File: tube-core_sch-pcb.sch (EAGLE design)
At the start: 14 parts

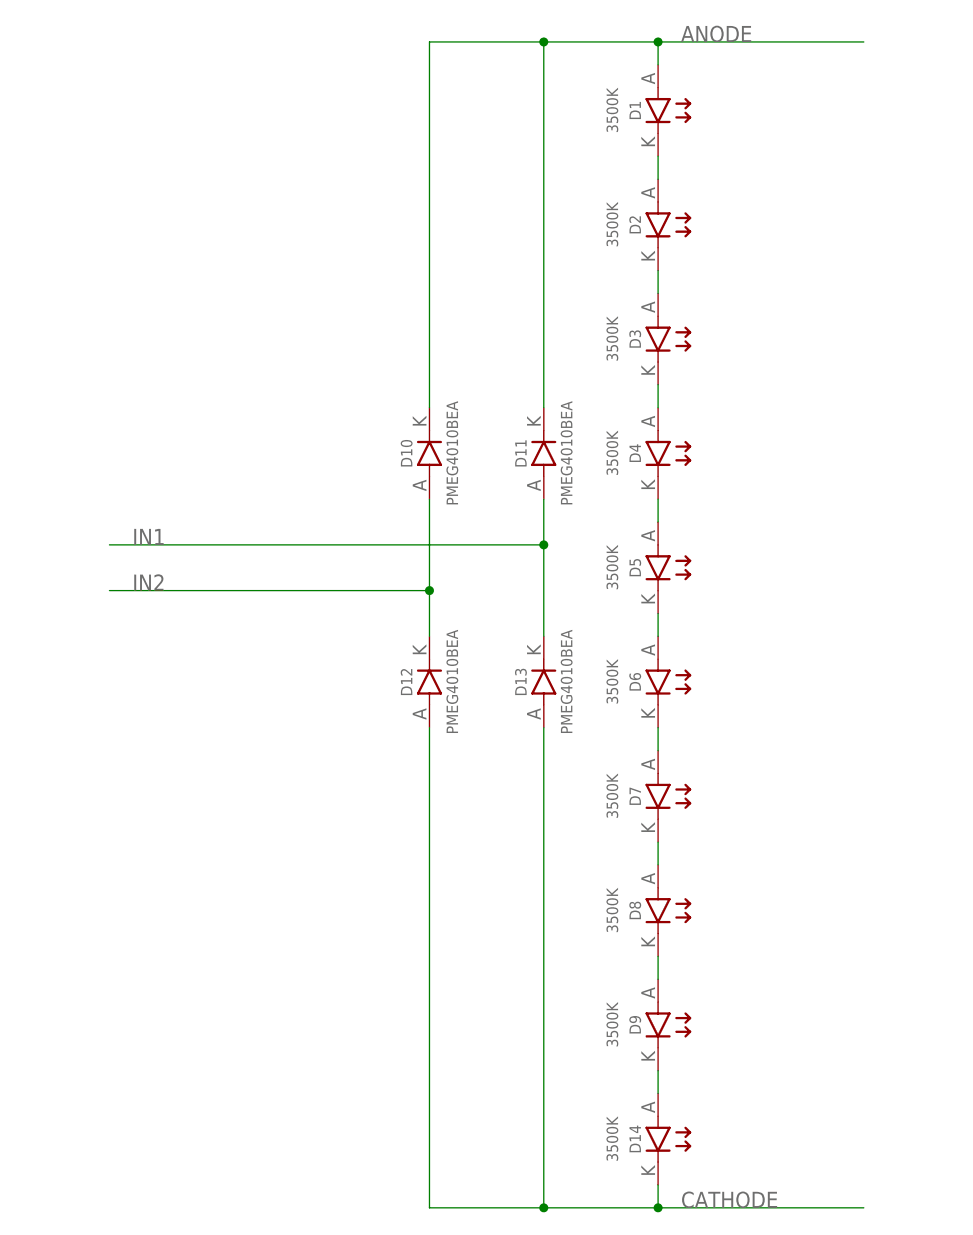
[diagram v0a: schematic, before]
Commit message: Recreated core with new diodes
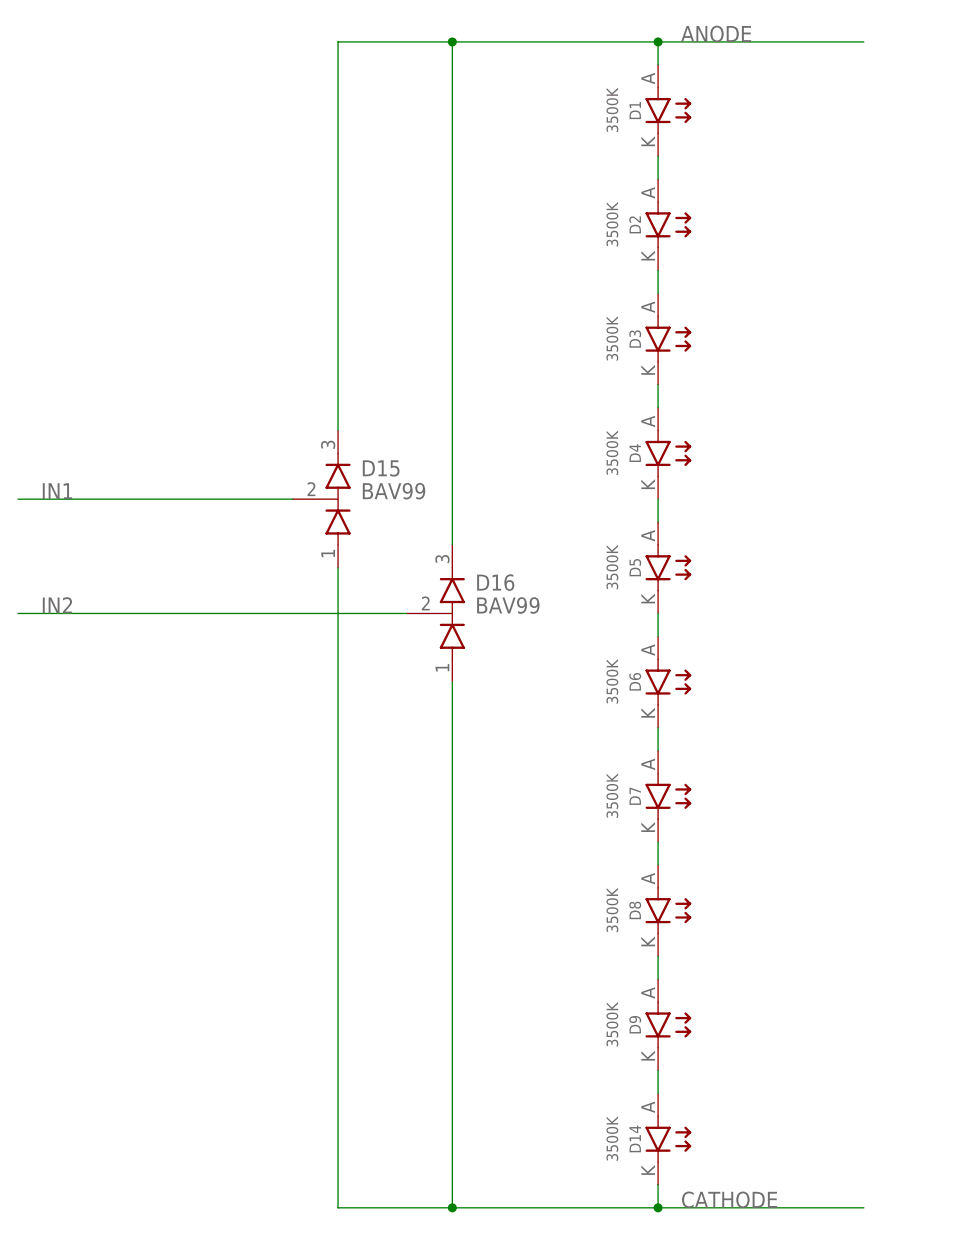
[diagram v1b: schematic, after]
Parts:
- removed D10, D11, D12, D13: PMEG4010BEA, DIODES:PMEG4010BEA
- added D15, D16: BAV99, DIODES:BAV99
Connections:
- net ANODE: now also D15.K, D16.K; no longer D10.K, D11.K
- net CATHODE: now also D15.A, D16.A; no longer D12.A, D13.A
- net IN1: now also D15.AK; no longer D11.A, D13.K
- net IN2: now also D16.AK; no longer D10.A, D12.K
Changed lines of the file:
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@@
 <part name="D8" library="OPTO" deviceset="JE2835AWT-00-0000-0B0A0UF735E" device="" value="3500K"/>
 <part name="D9" library="OPTO" deviceset="JE2835AWT-00-0000-0B0A0UF735E" device="" value="3500K"/>
-<part name="D10" library="DIODES" deviceset="PMEG4010BEA" device="" value="PMEG4010BEA"/>
-<part name="D11" library="DIODES" deviceset="PMEG4010BEA" device="" value="PMEG4010BEA"/>
-<part name="D12" library="DIODES" deviceset="PMEG4010BEA" device="" value="PMEG4010BEA"/>
-<part name="D13" library="DIODES" deviceset="PMEG4010BEA" device="" value="PMEG4010BEA"/>
 <part name="D14" library="OPTO" deviceset="JE2835AWT-00-0000-0B0A0UF735E" device="" value="3500K"/>
+<part name="D15" library="DIODES" deviceset="BAV99" device=""/>
+<part name="D16" library="DIODES" deviceset="BAV99" device=""/>
 </parts>
 <sheets>
@@
 <attribute name="VALUE" x="-5.08" y="-50.8" size="1.27" layer="96" rot="R270" align="center"/>
 </instance>
-<instance part="D10" gate="G$1" x="-25.4" y="12.7" smashed="yes" rot="R90">
-<attribute name="NAME" x="-27.94" y="12.7" size="1.27" layer="95" rot="R90" align="center"/>
-<attribute name="VALUE" x="-22.86" y="12.7" size="1.27" layer="96" rot="R90" align="center"/>
-</instance>
-<instance part="D11" gate="G$1" x="-12.7" y="12.7" smashed="yes" rot="R90">
-<attribute name="NAME" x="-15.24" y="12.7" size="1.27" layer="95" rot="R90" align="center"/>
-<attribute name="VALUE" x="-10.16" y="12.7" size="1.27" layer="96" rot="R90" align="center"/>
-</instance>
-<instance part="D12" gate="G$1" x="-25.4" y="-12.7" smashed="yes" rot="R90">
-<attribute name="NAME" x="-27.94" y="-12.7" size="1.27" layer="95" rot="R90" align="center"/>
-<attribute name="VALUE" x="-22.86" y="-12.7" size="1.27" layer="96" rot="R90" align="center"/>
-</instance>
-<instance part="D13" gate="G$1" x="-12.7" y="-12.7" smashed="yes" rot="R90">
-<attribute name="NAME" x="-15.24" y="-12.7" size="1.27" layer="95" rot="R90" align="center"/>
-<attribute name="VALUE" x="-10.16" y="-12.7" size="1.27" layer="96" rot="R90" align="center"/>
-</instance>
 <instance part="D14" gate="G$1" x="0" y="-63.5" smashed="yes" rot="R270">
 <attribute name="NAME" x="-2.54" y="-63.5" size="1.27" layer="95" rot="R270" align="center"/>
 <attribute name="VALUE" x="-5.08" y="-63.5" size="1.27" layer="96" rot="R270" align="center"/>
+</instance>
+<instance part="D15" gate="G$1" x="-35.56" y="7.62" smashed="yes">
+<attribute name="NAME" x="-33.02" y="10.16" size="1.778" layer="95"/>
+<attribute name="VALUE" x="-33.02" y="7.62" size="1.778" layer="96"/>
+</instance>
+<instance part="D16" gate="G$1" x="-22.86" y="-5.08" smashed="yes">
+<attribute name="NAME" x="-20.32" y="-2.54" size="1.778" layer="95"/>
+<attribute name="VALUE" x="-20.32" y="-5.08" size="1.778" layer="96"/>
 </instance>
 </instances>
@@
 <net name="IN1" class="0">
 <segment>
-<pinref part="D11" gate="G$1" pin="A"/>
-<pinref part="D13" gate="G$1" pin="K"/>
-<wire x1="-12.7" y1="7.62" x2="-12.7" y2="2.54" width="0.1524" layer="91"/>
-<wire x1="-12.7" y1="2.54" x2="-12.7" y2="-7.62" width="0.1524" layer="91"/>
-<wire x1="-12.7" y1="2.54" x2="-60.96" y2="2.54" width="0.1524" layer="91"/>
-<junction x="-12.7" y="2.54"/>
-<label x="-58.42" y="2.54" size="1.778" layer="95"/>
+<label x="-68.58" y="7.62" size="1.778" layer="95"/>
+<wire x1="-40.64" y1="7.62" x2="-71.12" y2="7.62" width="0.1524" layer="91"/>
+<pinref part="D15" gate="G$1" pin="AK"/>
 </segment>
 </net>
 <net name="IN2" class="0">
 <segment>
-<pinref part="D10" gate="G$1" pin="A"/>
-<pinref part="D12" gate="G$1" pin="K"/>
-<wire x1="-25.4" y1="7.62" x2="-25.4" y2="-2.54" width="0.1524" layer="91"/>
-<wire x1="-25.4" y1="-2.54" x2="-25.4" y2="-7.62" width="0.1524" layer="91"/>
-<wire x1="-25.4" y1="-2.54" x2="-60.96" y2="-2.54" width="0.1524" layer="91"/>
-<junction x="-25.4" y="-2.54"/>
-<label x="-58.42" y="-2.54" size="1.778" layer="95"/>
+<label x="-68.58" y="-5.08" size="1.778" layer="95"/>
+<pinref part="D16" gate="G$1" pin="AK"/>
+<wire x1="-71.12" y1="-5.08" x2="-27.94" y2="-5.08" width="0.1524" layer="91"/>
 </segment>
 </net>
 <net name="ANODE" class="0">
 <segment>
-<pinref part="D10" gate="G$1" pin="K"/>
-<wire x1="-25.4" y1="17.78" x2="-25.4" y2="58.42" width="0.1524" layer="91"/>
-<wire x1="-25.4" y1="58.42" x2="-12.7" y2="58.42" width="0.1524" layer="91"/>
+<wire x1="-35.56" y1="15.24" x2="-35.56" y2="58.42" width="0.1524" layer="91"/>
+<wire x1="-35.56" y1="58.42" x2="-22.86" y2="58.42" width="0.1524" layer="91"/>
 <pinref part="D1" gate="G$1" pin="A"/>
-<wire x1="-12.7" y1="58.42" x2="0" y2="58.42" width="0.1524" layer="91"/>
+<wire x1="-22.86" y1="58.42" x2="0" y2="58.42" width="0.1524" layer="91"/>
 <wire x1="0" y1="58.42" x2="0" y2="55.88" width="0.1524" layer="91"/>
-<pinref part="D11" gate="G$1" pin="K"/>
-<wire x1="-12.7" y1="17.78" x2="-12.7" y2="58.42" width="0.1524" layer="91"/>
-<junction x="-12.7" y="58.42"/>
+<wire x1="-22.86" y1="2.54" x2="-22.86" y2="58.42" width="0.1524" layer="91"/>
+<junction x="-22.86" y="58.42"/>
 <label x="2.54" y="58.42" size="1.778" layer="95"/>
 <wire x1="0" y1="58.42" x2="22.86" y2="58.42" width="0.1524" layer="91"/>
 <junction x="0" y="58.42"/>
+<pinref part="D15" gate="G$1" pin="K"/>
+<pinref part="D16" gate="G$1" pin="K"/>
 </segment>
 </net>
 <net name="CATHODE" class="0">
 <segment>
-<pinref part="D12" gate="G$1" pin="A"/>
-<wire x1="-25.4" y1="-17.78" x2="-25.4" y2="-71.12" width="0.1524" layer="91"/>
-<wire x1="-25.4" y1="-71.12" x2="-12.7" y2="-71.12" width="0.1524" layer="91"/>
-<wire x1="-12.7" y1="-71.12" x2="0" y2="-71.12" width="0.1524" layer="91"/>
+<wire x1="-35.56" y1="0" x2="-35.56" y2="-71.12" width="0.1524" layer="91"/>
+<wire x1="-35.56" y1="-71.12" x2="-22.86" y2="-71.12" width="0.1524" layer="91"/>
+<wire x1="-22.86" y1="-71.12" x2="0" y2="-71.12" width="0.1524" layer="91"/>
 <wire x1="0" y1="-71.12" x2="22.86" y2="-71.12" width="0.1524" layer="91"/>
 <junction x="0" y="-71.12"/>
-<pinref part="D13" gate="G$1" pin="A"/>
-<wire x1="-12.7" y1="-17.78" x2="-12.7" y2="-71.12" width="0.1524" layer="91"/>
-<junction x="-12.7" y="-71.12"/>
+<wire x1="-22.86" y1="-12.7" x2="-22.86" y2="-71.12" width="0.1524" layer="91"/>
+<junction x="-22.86" y="-71.12"/>
 <label x="2.54" y="-71.12" size="1.778" layer="95"/>
 <wire x1="0" y1="-68.58" x2="0" y2="-71.12" width="0.1524" layer="91"/>
 <pinref part="D14" gate="G$1" pin="K"/>
+<pinref part="D15" gate="G$1" pin="A"/>
+<pinref part="D16" gate="G$1" pin="A"/>
 </segment>
 </net>

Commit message: Tube core complete
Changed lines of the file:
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@@
 <?xml version="1.0" encoding="utf-8"?>
 <!DOCTYPE eagle SYSTEM "eagle.dtd">
-<eagle version="9.3.0">
+<eagle version="9.3.2">
 <drawing>
 <settings>
@@
 <part name="D9" library="OPTO" deviceset="JE2835AWT-00-0000-0B0A0UF735E" device="" value="3500K"/>
 <part name="D14" library="OPTO" deviceset="JE2835AWT-00-0000-0B0A0UF735E" device="" value="3500K"/>
-<part name="D15" library="DIODES" deviceset="BAV99" device=""/>
-<part name="D16" library="DIODES" deviceset="BAV99" device=""/>
+<part name="D15" library="DIODES" deviceset="BAV99" device="" value="BAV99"/>
+<part name="D16" library="DIODES" deviceset="BAV99" device="" value="BAV99"/>
 </parts>
 <sheets>

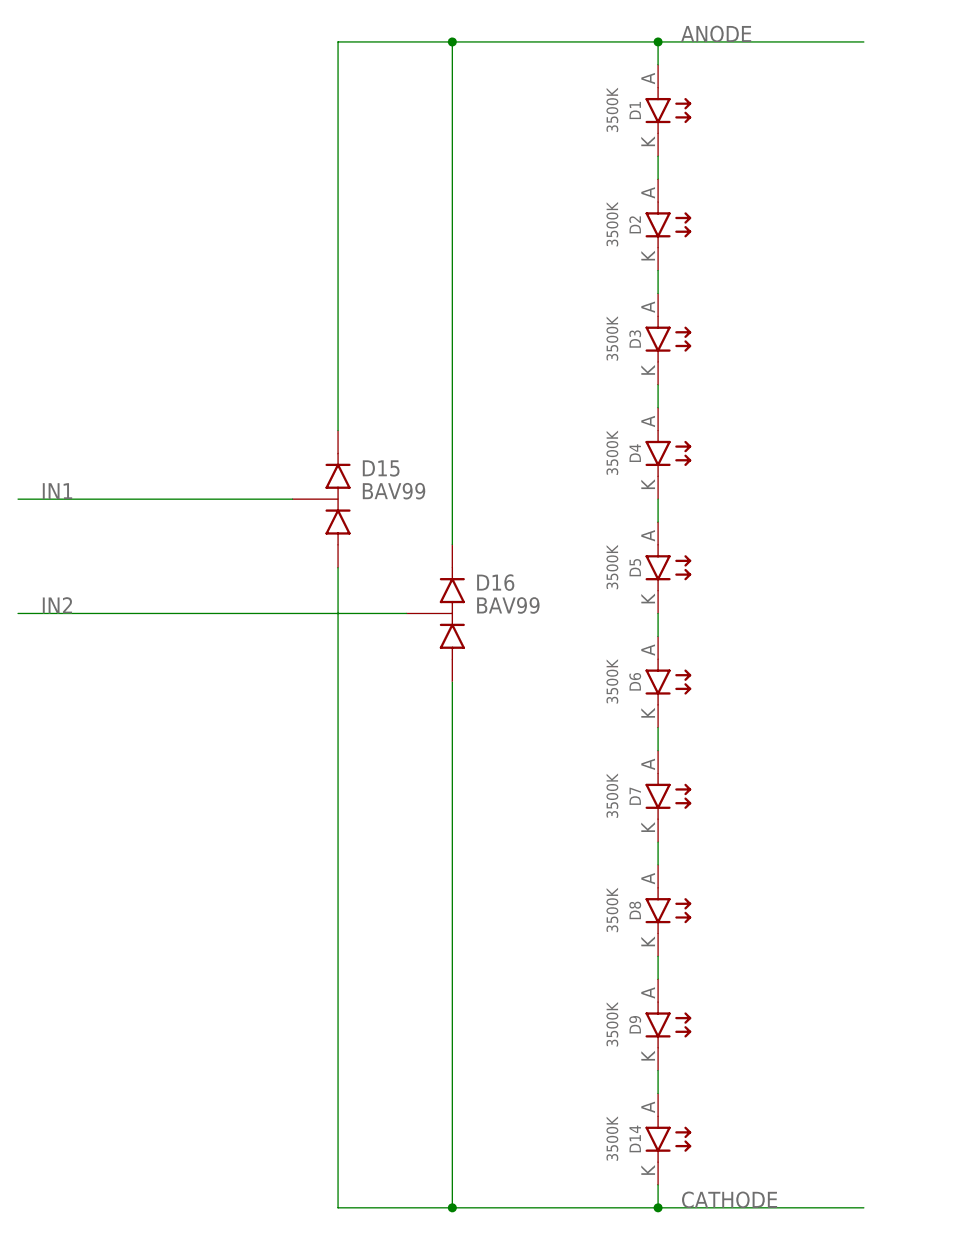
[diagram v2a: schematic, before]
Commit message: New LED design
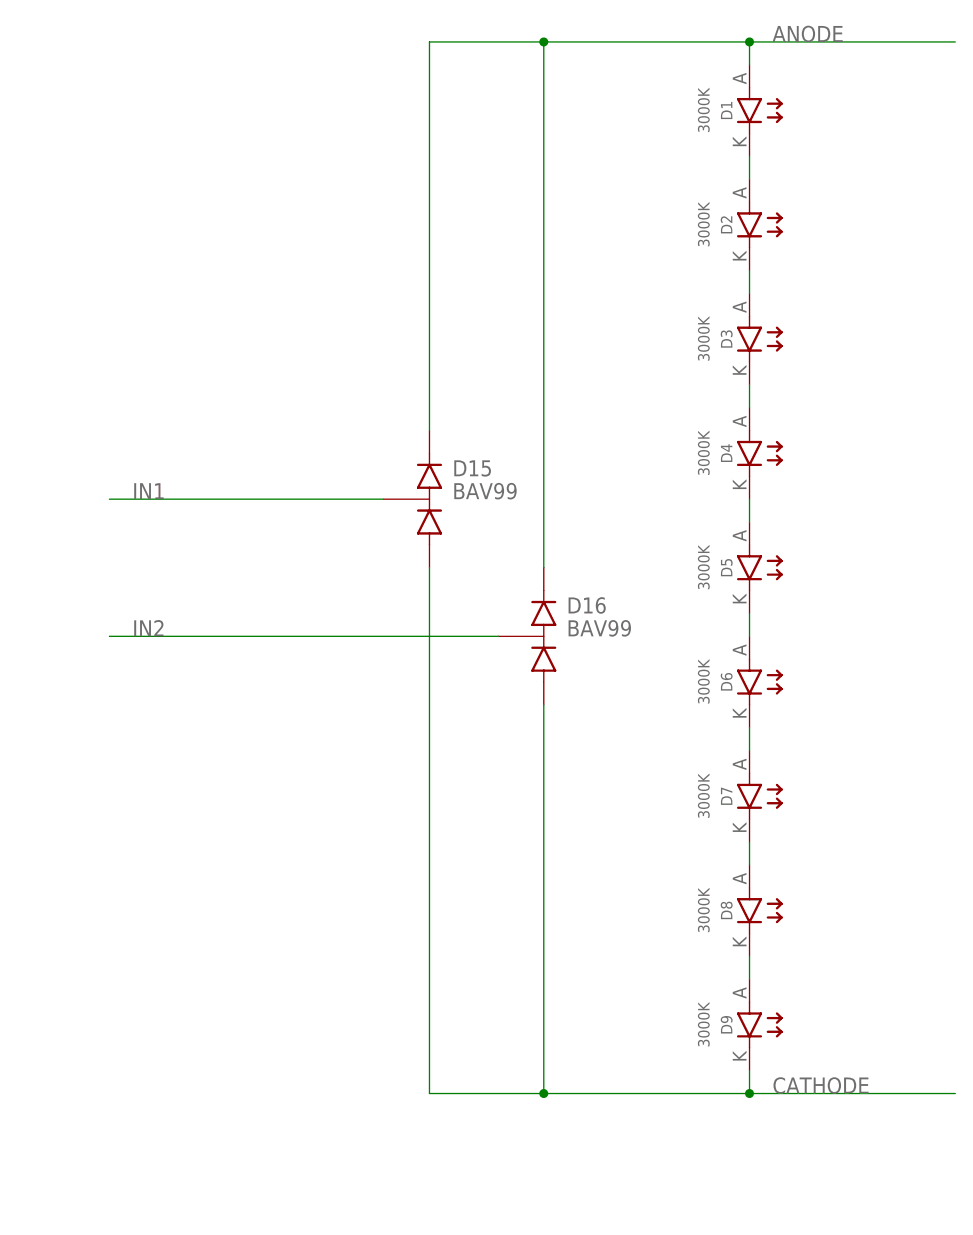
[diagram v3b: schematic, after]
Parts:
- removed D14: 3500K, OPTO:JE2835AWT-00-0000-0B0A0UF735E
- D1, D2, D3, D4, D5, D6, D7, D8, D9: value 3500K -> 3000K; device OPTO:JE2835AWT-00-0000-0B0A0UF735E -> OPTO:MP-1616-1100-30-90
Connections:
- removed net N$7 (its old number): D14.A, D9.K
- net CATHODE: now also D9.K; no longer D14.K
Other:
- moved on the sheet: D1, D15, D16, D2, D3, D4, D5, D6, D7, D8, D9
